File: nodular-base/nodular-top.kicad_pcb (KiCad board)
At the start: 2 copper layers, 83.1 x 92.5 mm, 39 parts, among them J1 Conn_01x30_MountingPin, SW1 SW_Push, SW2 SW_Push, SW3 SW_Push, SW4 SW_Push, SW5 SW_Push, SW6 SW_Push

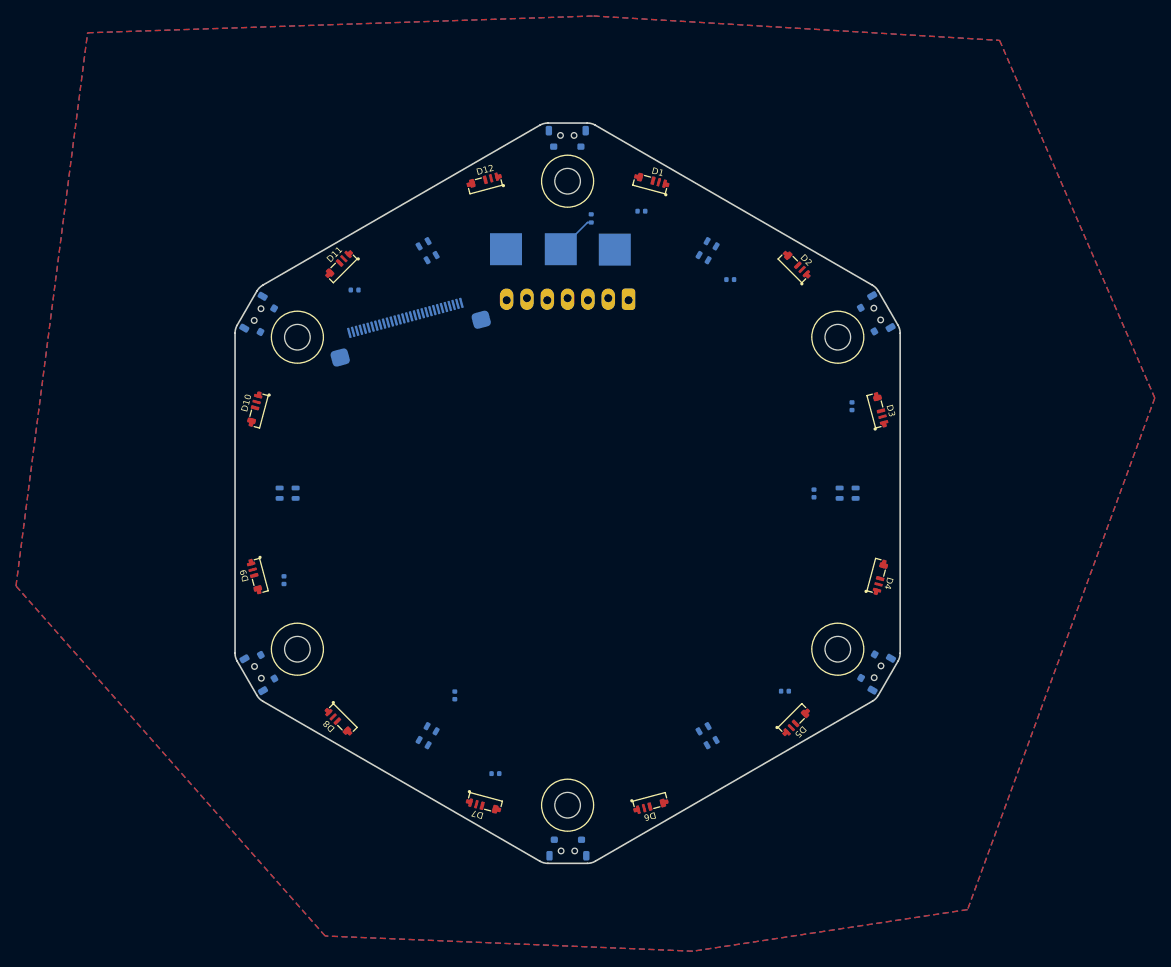
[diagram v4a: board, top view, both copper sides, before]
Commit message: Add eeprom and complete top electrical connections
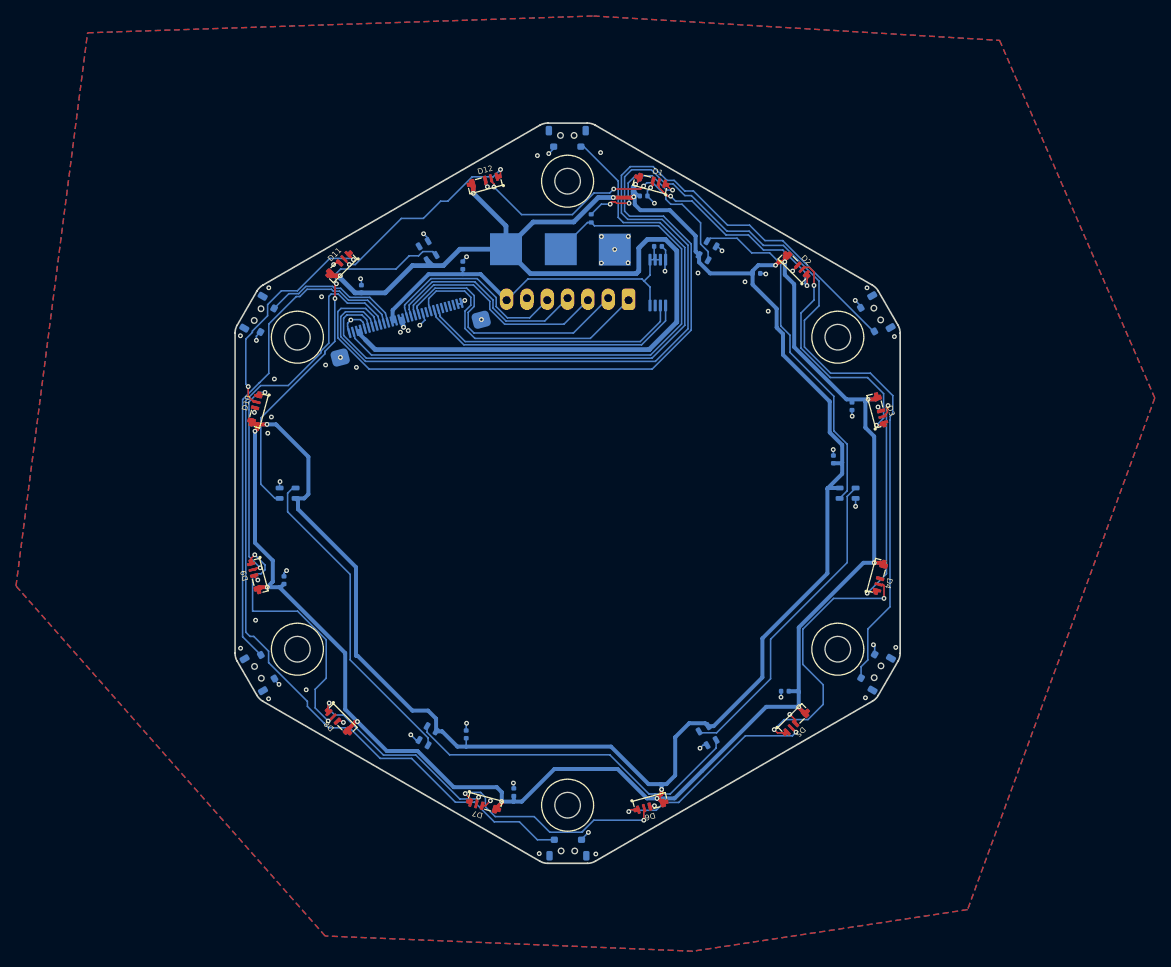
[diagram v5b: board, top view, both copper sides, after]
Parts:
- added C10: 1u, Capacitor_SMD:C_0402_1005Metric, B.Cu at (111.3, 69.2)
- added C11: 1u, Capacitor_SMD:C_0402_1005Metric, B.Cu at (86.9, 71.5)
- added U2: 24LC00, Package_SO:TSSOP-8_4.4x3mm_P0.65mm, B.Cu at (111.3, 73.7)
- moved C8 5.08 mm to (87.3, 130.1), turned to 90 degrees
- moved C9 4.90 mm to (133.2, 95.8), turned to 90 degrees
- moved C7 3.36 mm to (123.6, 72.5)
- moved C4 3.27 mm to (93.3, 137.4), turned to 90 degrees
- moved C1 1.92 mm to (109.5, 62.9)
- moved C6 0.85 mm to (74.2, 74.5), turned to 90 degrees
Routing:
- net /VBAT_SW: track 0.00 -> 527.2 mm, vias 0 -> 17
- net /BTN3: track 0.00 -> 172.4 mm
- net /BTN2: track 0.00 -> 120.0 mm
- net /BTN4: track 0.00 -> 107.3 mm
- net /BTN1: track 0.00 -> 82.6 mm
- net /LED_DATA: track 5.18 -> 71.6 mm
- net /BTN5: track 0.00 -> 62.1 mm
- net /3V3: track 0.00 -> 47.8 mm
- net Net-(D17-DOUT): track 0.00 -> 47.2 mm, vias 0 -> 2
- net GND: track 0.00 -> 45.6 mm, vias 0 -> 70
- net Net-(D13-DOUT): track 0.00 -> 43.8 mm
- net Net-(D15-DOUT): track 0.00 -> 43.5 mm
- net Net-(D14-DOUT): track 0.00 -> 40.1 mm
- net Net-(D16-DOUT): track 0.00 -> 40.0 mm
- net Net-(D12-DOUT): track 0.00 -> 37.5 mm, vias 0 -> 3
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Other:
- board text added: "BATTERY GOES HERE"
- board text added: "^ RIBBON HERE ^ Contacts towards board Plug in before placing battery"

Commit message: Add baseline art (bart), add stencil alignment holes, complete BOM, prepare for proto order
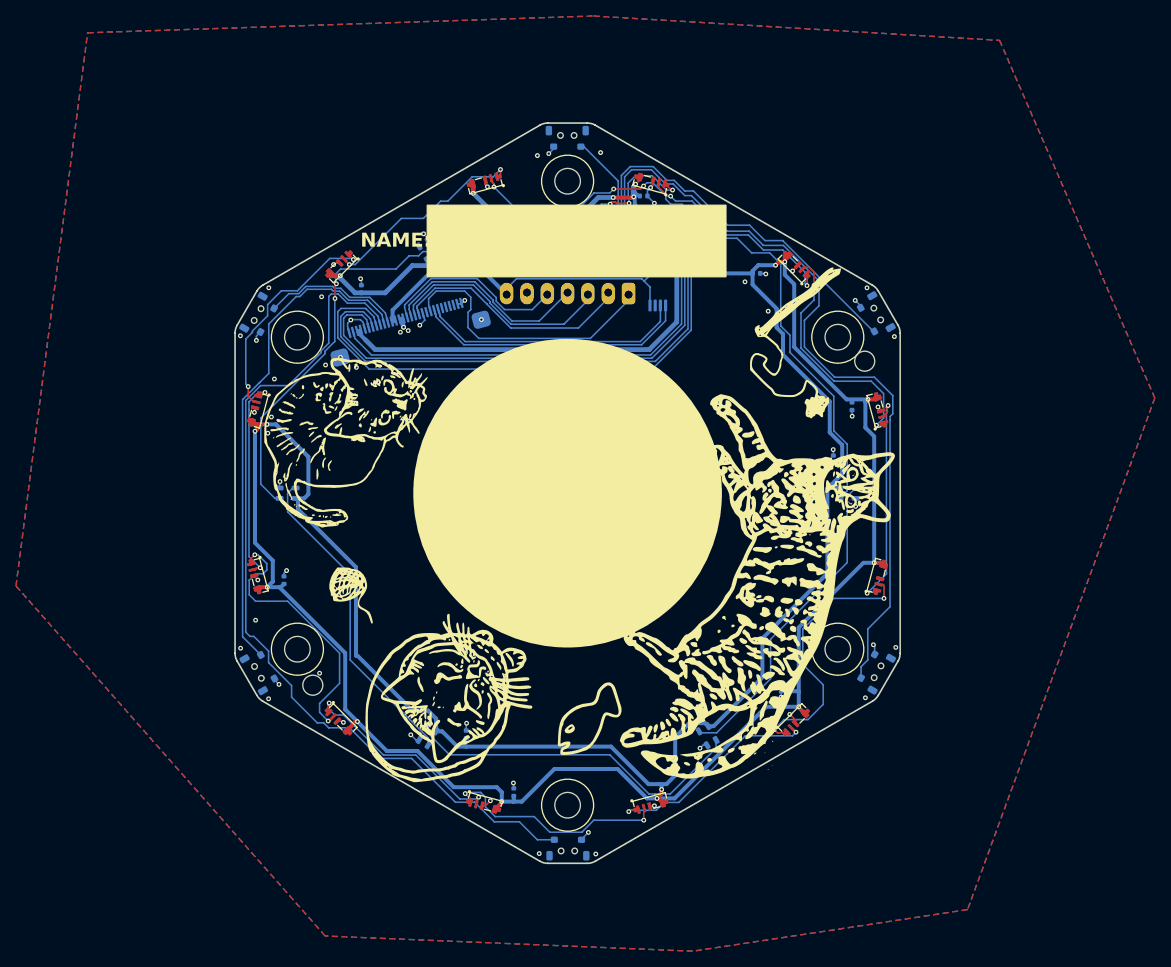
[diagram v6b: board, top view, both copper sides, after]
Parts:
- added G***: LOGO, nodular:cats-silk, F.Cu at (99.3, 100.2)
- moved U1 0.70 mm to (100.0, 75.0)
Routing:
- net /HS4: track 33.4 -> 29.5 mm
- net /HS1: track 24.4 -> 23.4 mm
- net Net-(D8-DOUT): track 32.6 -> 33.5 mm
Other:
- outline, holes or cut-outs redrawn
- board text added: "ELECTRO MAGNETIC FELINES"
- board text added: "NAME:"
- board text added: "Prototype Dec23"

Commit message: Modify base board: - Fix ESP32 strapping pins state - Remove 3/6 M3 standoffs - Change to LGA-style pads on ESP32 - Modify SFP mechanical pads to not be plated - Add larger mechanical pads with more solder paste surface to USB-C connectors
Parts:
- added REF**: TestPoint_Pad_D1.0mm, TestPoint:TestPoint_Pad_D1.0mm, B.Cu at (100.0, 100.0)
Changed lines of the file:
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@@
+    )
+  )
+  (footprint "TestPoint:TestPoint_Pad_D1.0mm" (layer "B.Cu")
+    (at 100 100 180)
+    (descr "SMD pad as test Point, diameter 1.0mm")
+    (tags "test point SMD pad")
+    (attr exclude_from_pos_files exclude_from_bom)
+    (fp_text reference "REF**" (at 0 1.448) (layer "B.SilkS") hide
+        (effects (font (size 1 1) (thickness 0.15)) (justify mirror))
+    )
+    (fp_text value "TestPoint_Pad_D1.0mm" (at 0 -1.55) (layer "B.Fab") hide
+        (effects (font (size 1 1) (thickness 0.15)) (justify mirror))
+    )
+    (fp_text user "${REFERENCE}" (at 0 1.45) (layer "B.Fab")
+        (effects (font (size 1 1) (thickness 0.15)) (justify mirror))
+    )
+    (fp_circle (center 0 0) (end 1 0)
+      (stroke (width 0.05) (type solid)) (fill none) (layer "B.CrtYd"))
+    (model "${KIPRJMOD}/3d/battery.stepx"
+      (offset (xyz -0.5 -2 0.5))
+      (scale (xyz 1 1 1))
+      (rotate (xyz 0 0 -165))
+    )
+    (model "${KIPRJMOD}/nodular-bottom.stepx"
+      (offset (xyz 0 0 14.6))
+      (scale (xyz 1 1 1))
+      (rotate (xyz 0 -180 0))
     )
   )

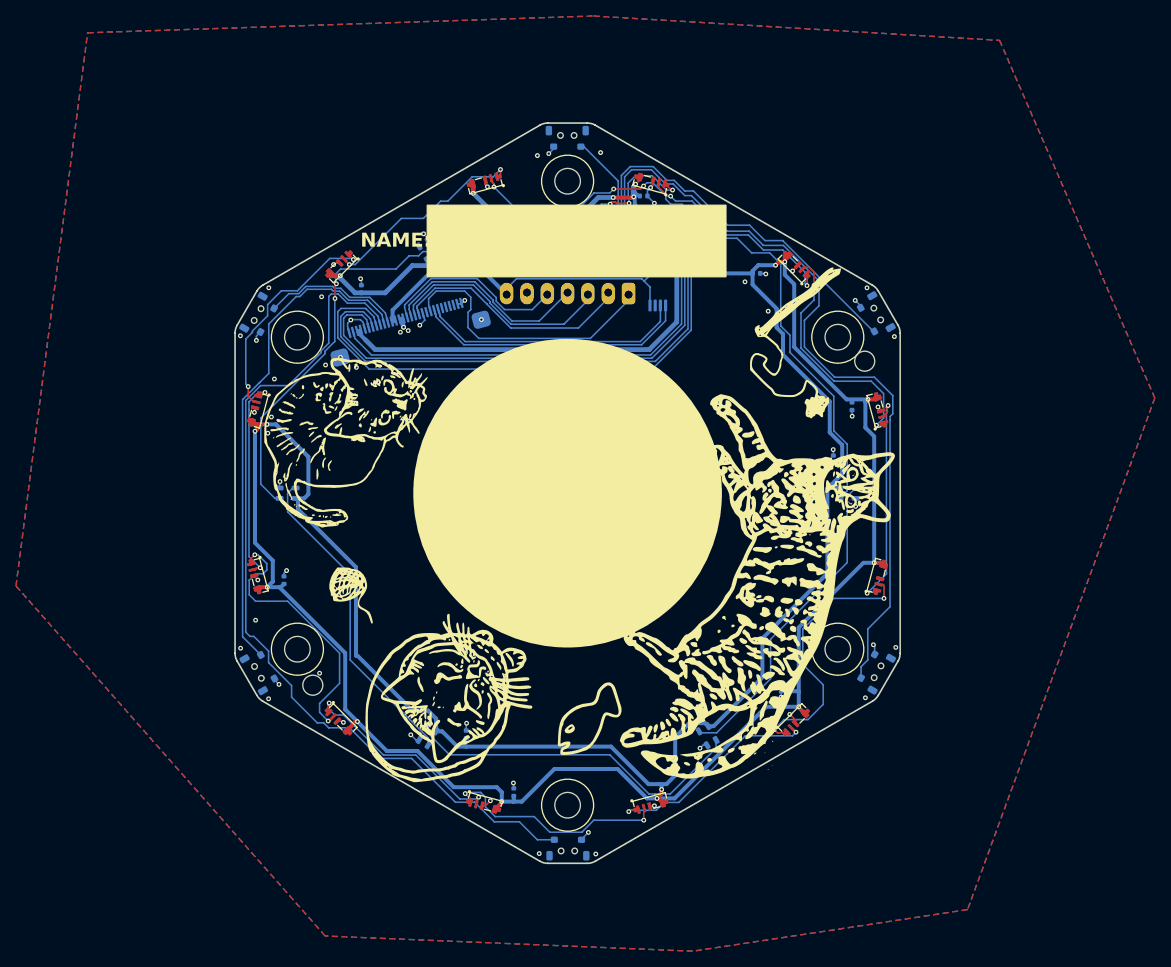
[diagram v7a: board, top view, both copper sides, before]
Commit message: Update top board layout, rename libraries
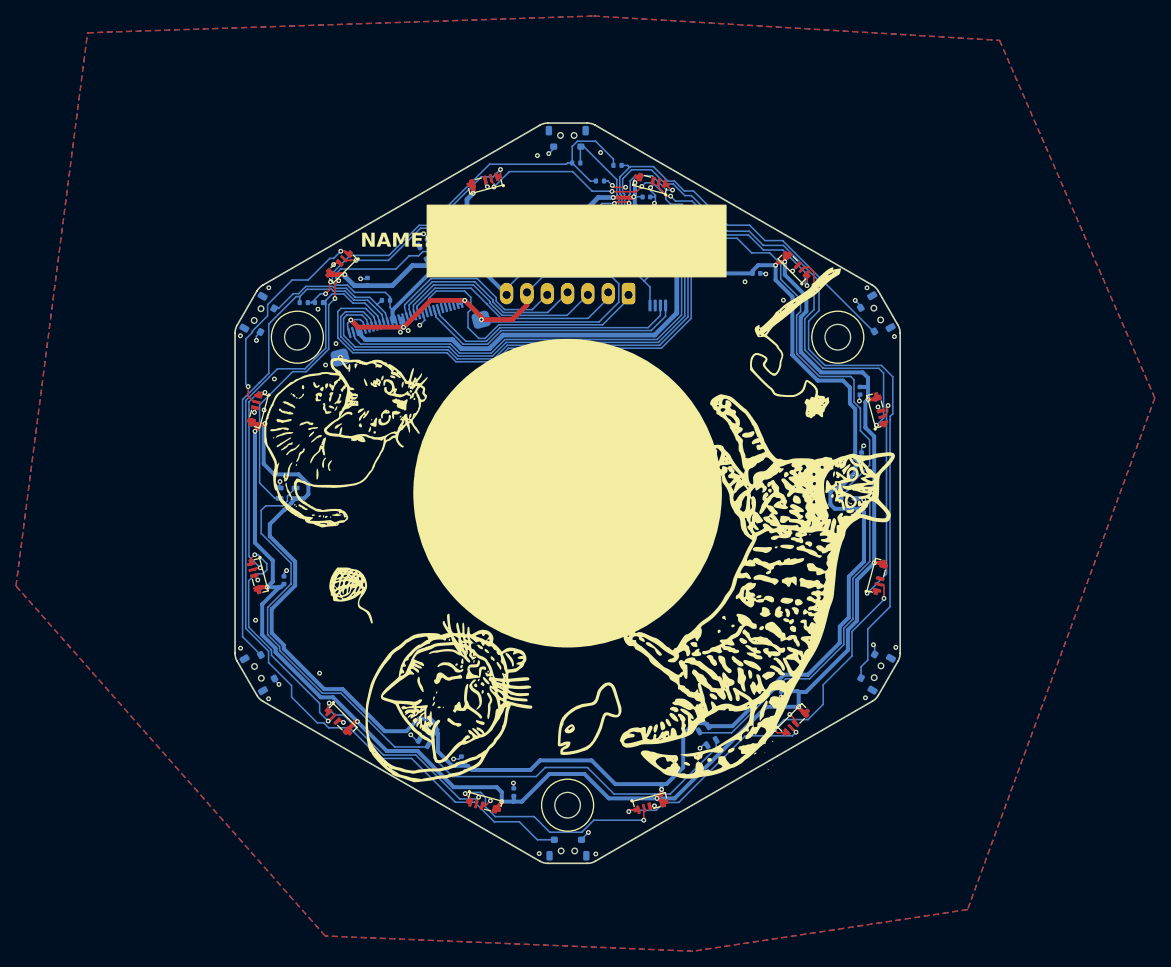
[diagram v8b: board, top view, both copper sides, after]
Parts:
- removed REF**: TestPoint_Pad_D1.0mm, TestPoint:TestPoint_Pad_D1.0mm
- removed TP1, TP2, TP3: TestPoint, TestPoint:TestPoint_Pad_4.0x4.0mm
- added R2: 100k, Resistor_SMD:R_0402_1005Metric, B.Cu at (77.3, 75.9)
- added R3: 100k, Resistor_SMD:R_0402_1005Metric, B.Cu at (67.0, 76.2)
- added R4: 100k, Resistor_SMD:R_0402_1005Metric, B.Cu at (68.9, 76.2)
- added R5: 100k, Resistor_SMD:R_0402_1005Metric, B.Cu at (104.0, 61.0)
- added R6: 100k, Resistor_SMD:R_0402_1005Metric, B.Cu at (106.2, 59.0)
- added R7: 100k, Resistor_SMD:R_0402_1005Metric, B.Cu at (101.1, 58.7)
- moved C9 3.54 mm to (136.8, 95.4)
- moved C8 3.31 mm to (86.7, 133.4)
- moved C2 2.17 mm to (136.6, 87.2)
- moved C6 1.18 mm to (75.0, 73.6)
- moved C1 0.37 mm to (109.8, 63.0)
- turned D15 to -60 degrees
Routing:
- net /3V3: track 47.7 -> 113.3 mm, vias 0 -> 2
- net GND: track 45.6 -> 106.1 mm, vias 70 -> 64
- net /VBAT_SW: track 527.2 -> 548.6 mm, vias 17 -> 18
- net Net-(D16-DOUT): track 40.0 -> 50.4 mm
- net /LED_DATA: track 71.6 -> 65.5 mm
- net Net-(D4-DOUT): track 33.6 -> 27.8 mm
- net Net-(D14-DOUT): track 40.1 -> 45.1 mm
- net Net-(D13-DOUT): track 43.8 -> 48.8 mm
- net Net-(D8-DOUT): track 33.5 -> 29.2 mm
- net /BTN3: track 172.4 -> 175.2 mm, vias 0 -> 2
- net Net-(D15-DOUT): track 43.5 -> 45.8 mm
- net Net-(D17-DOUT): track 47.2 -> 48.6 mm
- net /HS3: track 28.2 -> 26.9 mm
- net /BTN1: track 82.6 -> 83.8 mm
- net Net-(D10-DOUT): track 28.2 -> 27.1 mm
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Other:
- outline, holes or cut-outs redrawn
- board text removed: "LED_DATA"
- board text removed: "LED_PWR"
